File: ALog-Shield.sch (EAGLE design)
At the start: 32 parts

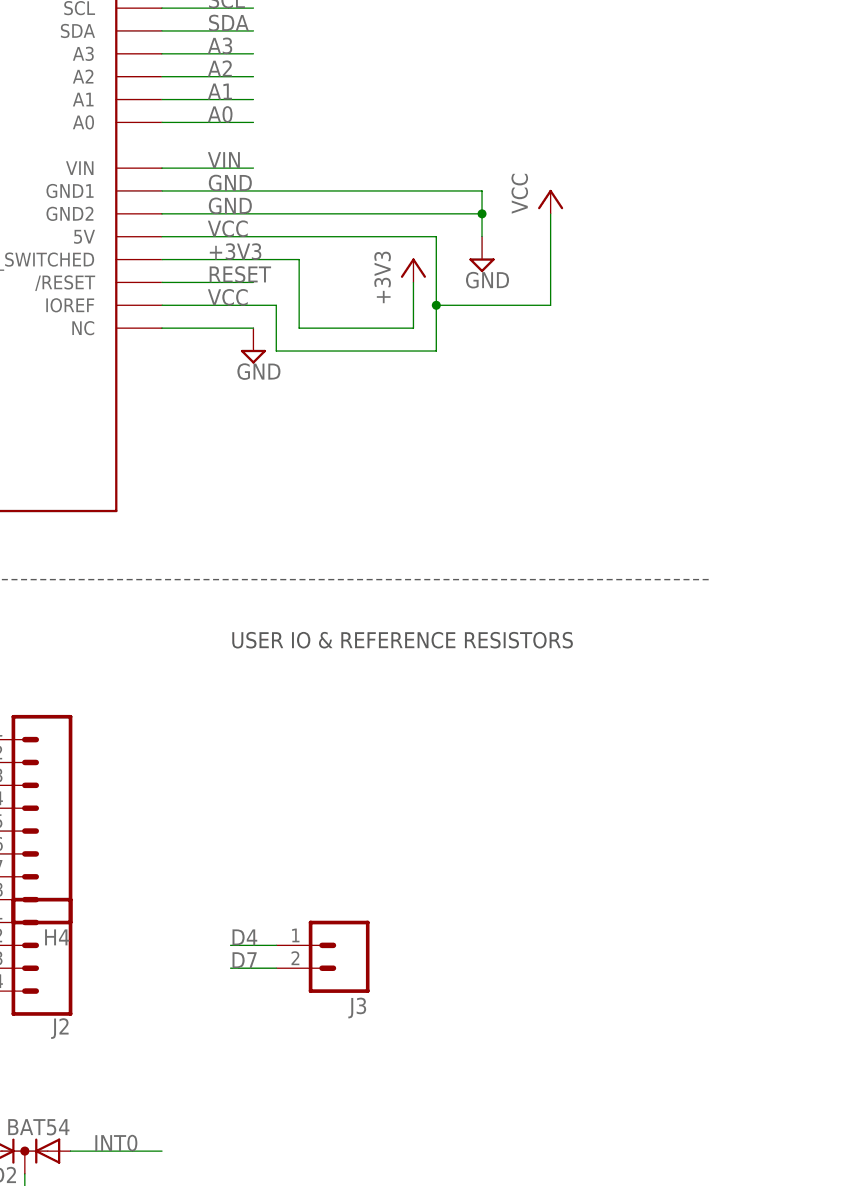
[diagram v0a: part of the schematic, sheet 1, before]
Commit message: IO Ref conversion
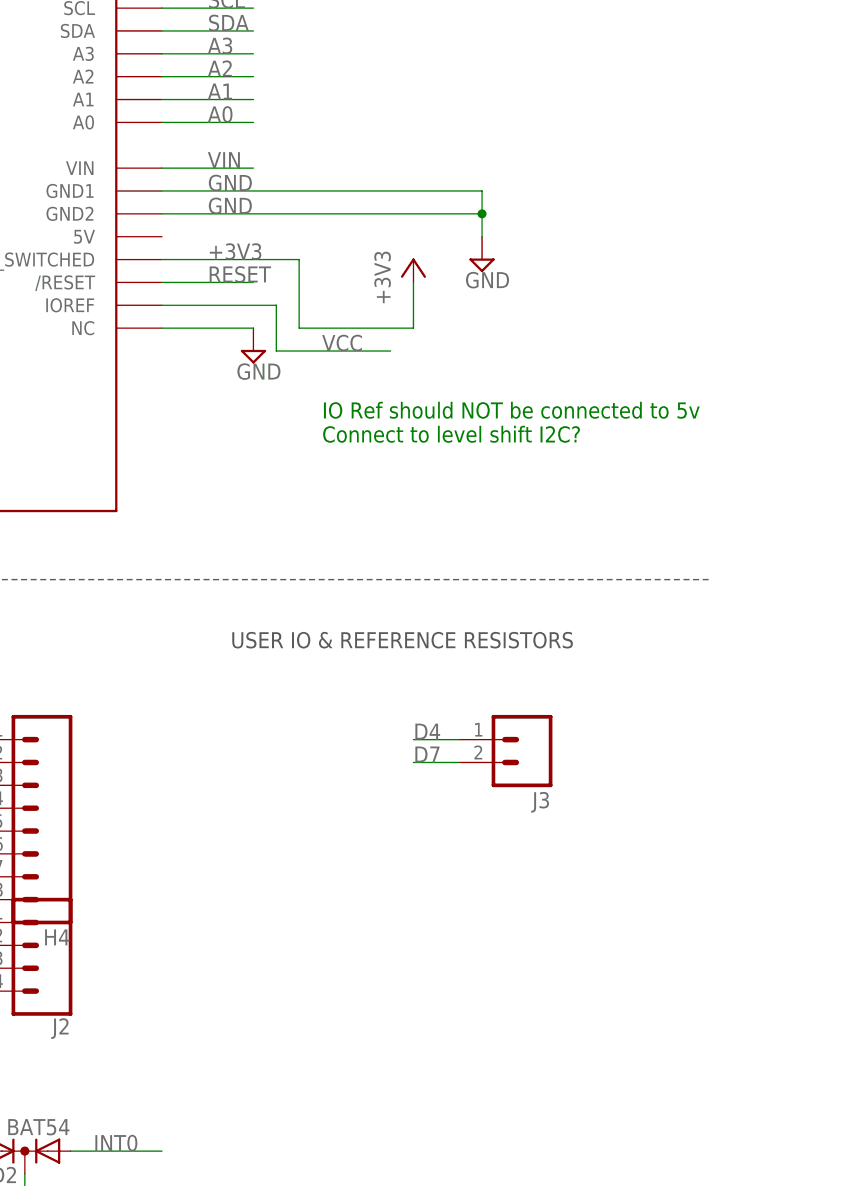
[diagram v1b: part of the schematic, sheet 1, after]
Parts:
- removed R_PU_A, R_PU_L: 10k, bschulz_passives:R-EU_10KR0603
- added R1, R2: 10k, bschulz:R-EU_R0603
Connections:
- net SCL: now also R1.1; no longer R_PU_L.2
- net SDA: now also R2.1; no longer R_PU_A.2
- net VCC: now also R1.2, R2.2; no longer R_PU_A.1, R_PU_L.1, U$9.5V
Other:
- note added: "IO Ref should NOT be connected to 5v Connect to level shift I2C?"
- note added: "If level shifters are used, these pull ups should be removed!"
- moved on the sheet: J3
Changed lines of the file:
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@@
 <?xml version="1.0" encoding="utf-8"?>
 <!DOCTYPE eagle SYSTEM "eagle.dtd">
-<eagle version="8.6.0">
+<eagle version="8.5.1">
 <drawing>
 <settings>
@@
 <part name="SUPPLY38" library="supply2" deviceset="GND" device=""/>
 <part name="SUPPLY39" library="supply2" deviceset="GND" device=""/>
-<part name="P+8" library="supply1" deviceset="VCC" device=""/>
 <part name="SUPPLY40" library="supply2" deviceset="GND" device=""/>
 <part name="+3V5" library="supply1" deviceset="+3V3" device=""/>
@@
 <part name="SUPPLY1" library="supply2" deviceset="GND" device=""/>
 <part name="P+3" library="supply1" deviceset="VCC" device=""/>
-<part name="P+5" library="supply1" deviceset="VCC" device=""/>
-<part name="P+7" library="supply1" deviceset="VCC" device=""/>
 <part name="P+9" library="supply1" deviceset="VCC" device=""/>
 <part name="H4" library="SparkFun" deviceset="M08" device="3.5MM-8"/>
@@
 <part name="JP1" library="SparkFun-Connectors" deviceset="M02" device="LOCK"/>
 <part name="+3V3" library="supply1" deviceset="+3V3" device=""/>
-<part name="R_PU_L" library="bschulz_passives" deviceset="R-EU_" device="R0603" technology="10K" value="10k"/>
-<part name="R_PU_A" library="bschulz_passives" deviceset="R-EU_" device="R0603" technology="10K" value="10k"/>
 <part name="C1" library="bschulz_passives" deviceset="C-EU" device="C0603" technology="0.1UF"/>
 <part name="C2" library="bschulz_passives" deviceset="C-EU" device="C0603" technology="0.1UF"/>
@@
 <part name="C4" library="bschulz_passives" deviceset="C-EU" device="C0603" technology="0.1UF"/>
 <part name="RTC1" library="bschulz" deviceset="DS3231M" device=""/>
+<part name="R1" library="bschulz" deviceset="R-EU_" device="R0603" value="10k"/>
+<part name="R2" library="bschulz" deviceset="R-EU_" device="R0603" value="10k"/>
+<part name="P+1" library="supply1" library_urn="urn:adsk.eagle:library:371" deviceset="VCC" device=""/>
+<part name="P+4" library="supply1" library_urn="urn:adsk.eagle:library:371" deviceset="VCC" device=""/>
 </parts>
 <sheets>
@@
 Chad Sandell</text>
 <text x="90.17" y="-222.504" size="5.08" layer="97">ALOG</text>
+<text x="142.24" y="-81.28" size="1.778" layer="91">IO Ref should NOT be connected to 5v
+Connect to level shift I2C?</text>
 </plain>
 <instances>
@@
 <instance part="SUPPLY38" gate="GND" x="35.56" y="-76.2"/>
 <instance part="SUPPLY39" gate="GND" x="160.02" y="-60.96"/>
-<instance part="P+8" gate="VCC" x="167.64" y="-53.34"/>
 <instance part="SUPPLY40" gate="GND" x="134.62" y="-71.12"/>
 <instance part="+3V5" gate="G$1" x="152.4" y="-60.96"/>
@@
 <instance part="U$3" gate="G$1" x="25.4" y="-236.22"/>
 <instance part="LOGO1" gate="G$1" x="17.78" y="-12.7"/>
-<instance part="J3" gate="G$1" x="144.78" y="-137.16" rot="R180"/>
+<instance part="J3" gate="G$1" x="165.1" y="-114.3" rot="R180"/>
 <instance part="U$1" gate="G$1" x="17.78" y="-27.94"/>
 <instance part="C1" gate="G$1" x="48.26" y="-165.1" rot="R90"/>
@@
 <net name="VCC" class="0">
 <segment>
-<wire x1="124.46" y1="-58.42" x2="154.94" y2="-58.42" width="0.1524" layer="91"/>
-<pinref part="U$9" gate="G$1" pin="5V"/>
-<label x="129.54" y="-58.42" size="1.778" layer="95"/>
-<wire x1="154.94" y1="-58.42" x2="154.94" y2="-66.04" width="0.1524" layer="91"/>
-<wire x1="154.94" y1="-66.04" x2="167.64" y2="-66.04" width="0.1524" layer="91"/>
-<wire x1="167.64" y1="-66.04" x2="167.64" y2="-55.88" width="0.1524" layer="91"/>
-<pinref part="P+8" gate="VCC" pin="VCC"/>
-<wire x1="124.46" y1="-66.04" x2="137.16" y2="-66.04" width="0.1524" layer="91"/>
-<pinref part="U$9" gate="G$1" pin="IOREF"/>
-<label x="129.54" y="-66.04" size="1.778" layer="95"/>
-<wire x1="137.16" y1="-66.04" x2="137.16" y2="-71.12" width="0.1524" layer="91"/>
-<wire x1="137.16" y1="-71.12" x2="154.94" y2="-71.12" width="0.1524" layer="91"/>
-<wire x1="154.94" y1="-71.12" x2="154.94" y2="-66.04" width="0.1524" layer="91"/>
-<junction x="154.94" y="-66.04"/>
-</segment>
-<segment>
 <label x="91.44" y="-124.46" size="1.778" layer="95"/>
 <wire x1="86.36" y1="-124.46" x2="104.14" y2="-124.46" width="0.1524" layer="91"/>
@@
 <pinref part="J1" gate="G$1" pin="1"/>
 <pinref part="P+2" gate="VCC" pin="VCC"/>
+</segment>
+<segment>
+<pinref part="U$9" gate="G$1" pin="IOREF"/>
+<wire x1="124.46" y1="-66.04" x2="137.16" y2="-66.04" width="0.1524" layer="91"/>
+<wire x1="137.16" y1="-66.04" x2="137.16" y2="-71.12" width="0.1524" layer="91"/>
+<wire x1="137.16" y1="-71.12" x2="149.86" y2="-71.12" width="0.1524" layer="91"/>
+<label x="142.24" y="-71.12" size="1.778" layer="95"/>
 </segment>
 </net>
@@
 <segment>
 <pinref part="J3" gate="G$1" pin="1"/>
-<wire x1="137.16" y1="-137.16" x2="132.08" y2="-137.16" width="0.1524" layer="91"/>
-<label x="132.08" y="-137.16" size="1.778" layer="95"/>
+<wire x1="157.48" y1="-114.3" x2="152.4" y2="-114.3" width="0.1524" layer="91"/>
+<label x="152.4" y="-114.3" size="1.778" layer="95"/>
 </segment>
 </net>
@@
 <segment>
 <pinref part="J3" gate="G$1" pin="2"/>
-<wire x1="137.16" y1="-139.7" x2="132.08" y2="-139.7" width="0.1524" layer="91"/>
-<label x="132.08" y="-139.7" size="1.778" layer="95"/>
+<wire x1="157.48" y1="-116.84" x2="152.4" y2="-116.84" width="0.1524" layer="91"/>
+<label x="152.4" y="-116.84" size="1.778" layer="95"/>
 </segment>
 </net>
@@
 <wire x1="104.14" y1="35.56" x2="104.14" y2="81.28" width="0.1524" layer="97" style="dashdot"/>
 <text x="114.3" y="76.2" size="1.778" layer="97">JUMPER: REFERENCE ANALOG TO 3V3 INSTEAD OF VCC</text>
+<text x="114.3" y="154.94" size="1.778" layer="91">If level shifters are used, these pull ups should be removed!</text>
 </plain>
 <instances>
@@
 <attribute name="DRAWING_NAME" x="101.6" y="19.05" size="2.54" layer="94"/>
 </instance>
-<instance part="P+5" gate="VCC" x="124.46" y="152.4"/>
-<instance part="P+7" gate="VCC" x="114.3" y="154.94"/>
 <instance part="P+9" gate="VCC" x="58.42" y="139.7"/>
 <instance part="CLOCK_BATT" gate="G$1" x="137.16" y="109.22" rot="R90"/>
@@
 <instance part="JP1" gate="G$1" x="129.54" y="58.42"/>
 <instance part="+3V3" gate="G$1" x="147.32" y="68.58"/>
-<instance part="R_PU_L" gate="G$1" x="114.3" y="142.24" rot="R270"/>
-<instance part="R_PU_A" gate="G$1" x="124.46" y="139.7" rot="R270"/>
 <instance part="RTC1" gate="G$1" x="78.74" y="132.08"/>
+<instance part="R1" gate="G$1" x="114.3" y="142.24" rot="R90"/>
+<instance part="R2" gate="G$1" x="124.46" y="139.7" rot="R90"/>
+<instance part="P+1" gate="VCC" x="114.3" y="152.4"/>
+<instance part="P+4" gate="VCC" x="124.46" y="149.86"/>
 </instances>
 <busses>
 </busses>
 <nets>
-<net name="VCC" class="0">
-<segment>
-<wire x1="124.46" y1="149.86" x2="124.46" y2="144.78" width="0.1524" layer="91"/>
-<pinref part="P+5" gate="VCC" pin="VCC"/>
-<pinref part="R_PU_A" gate="G$1" pin="1"/>
-</segment>
-<segment>
-<wire x1="114.3" y1="152.4" x2="114.3" y2="147.32" width="0.1524" layer="91"/>
-<pinref part="P+7" gate="VCC" pin="VCC"/>
-<pinref part="R_PU_L" gate="G$1" pin="1"/>
-</segment>
-<segment>
-<wire x1="66.04" y1="134.62" x2="58.42" y2="134.62" width="0.1524" layer="91"/>
-<wire x1="58.42" y1="134.62" x2="58.42" y2="137.16" width="0.1524" layer="91"/>
-<pinref part="P+9" gate="VCC" pin="VCC"/>
-<pinref part="RTC1" gate="G$1" pin="VCC"/>
-</segment>
-</net>
 <net name="DI" class="0">
 <segment>
@@
 </segment>
 </net>
-<net name="SCL" class="0">
-<segment>
-<wire x1="91.44" y1="137.16" x2="114.3" y2="137.16" width="0.1524" layer="91"/>
-<label x="99.06" y="137.16" size="1.778" layer="95"/>
-<pinref part="R_PU_L" gate="G$1" pin="2"/>
-<pinref part="RTC1" gate="G$1" pin="SCL"/>
-</segment>
-</net>
-<net name="SDA" class="0">
-<segment>
-<wire x1="91.44" y1="134.62" x2="124.46" y2="134.62" width="0.1524" layer="91"/>
-<label x="99.06" y="134.62" size="1.778" layer="95"/>
-<pinref part="R_PU_A" gate="G$1" pin="2"/>
-<pinref part="RTC1" gate="G$1" pin="SDA"/>
-</segment>
-</net>
 <net name="INT0" class="0">
 <segment>
@@
 </segment>
 </net>
+<net name="SCL" class="0">
+<segment>
+<wire x1="91.44" y1="137.16" x2="114.3" y2="137.16" width="0.1524" layer="91"/>
+<label x="99.06" y="137.16" size="1.778" layer="95"/>
+<pinref part="RTC1" gate="G$1" pin="SCL"/>
+<pinref part="R1" gate="G$1" pin="1"/>
+</segment>
+</net>
+<net name="SDA" class="0">
+<segment>
+<wire x1="91.44" y1="134.62" x2="124.46" y2="134.62" width="0.1524" layer="91"/>
+<label x="99.06" y="134.62" size="1.778" layer="95"/>
+<pinref part="RTC1" gate="G$1" pin="SDA"/>
+<pinref part="R2" gate="G$1" pin="1"/>
+</segment>
+</net>
+<net name="VCC" class="0">
+<segment>
+<wire x1="66.04" y1="134.62" x2="58.42" y2="134.62" width="0.1524" layer="91"/>
+<wire x1="58.42" y1="134.62" x2="58.42" y2="137.16" width="0.1524" layer="91"/>
+<pinref part="P+9" gate="VCC" pin="VCC"/>
+<pinref part="RTC1" gate="G$1" pin="VCC"/>
+</segment>
+<segment>
+<pinref part="R1" gate="G$1" pin="2"/>
+<pinref part="P+1" gate="VCC" pin="VCC"/>
+<wire x1="114.3" y1="147.32" x2="114.3" y2="149.86" width="0.1524" layer="91"/>
+</segment>
+<segment>
+<pinref part="R2" gate="G$1" pin="2"/>
+<pinref part="P+4" gate="VCC" pin="VCC"/>
+<wire x1="124.46" y1="144.78" x2="124.46" y2="147.32" width="0.1524" layer="91"/>
+</segment>
+</net>
 </nets>
 </sheet>
@@
 which will not be processed correctly with this version.
 </note>
+<note version="8.2" severity="warning">
+Since Version 8.2, EAGLE supports online libraries. The ids
+of those online libraries will not be understood (or retained)
+with this version.
+</note>
+<note version="8.3" severity="warning">
+Since Version 8.3, EAGLE supports URNs for individual library
+assets (packages, symbols, and devices). The URNs of those assets
+will not be understood (or retained) with this version.
+</note>
 </compatibility>

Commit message: PU, reroute, 5V terminal
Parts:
- removed J3: (no value), SparkFun-Connectors:M023.5MM
- added JP2: (no value), SparkFun-Connectors:M03SCREW
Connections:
- new net 5V: JP2.3, U$9.5V
- net D4: now also JP2.1; no longer J3.1
- net D7: now also JP2.2; no longer J3.2
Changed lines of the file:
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@@
 <?xml version="1.0" encoding="utf-8"?>
 <!DOCTYPE eagle SYSTEM "eagle.dtd">
-<eagle version="8.5.1">
+<eagle version="8.6.0">
 <drawing>
 <settings>
@@
 <part name="U$3" library="awickert" deviceset="ALOG_LOG" device=""/>
 <part name="LOGO1" library="SparkFun-Aesthetics" deviceset="OSHW-LOGO" device="L"/>
-<part name="J3" library="SparkFun-Connectors" deviceset="M02" device="3.5MM"/>
 <part name="+3V2" library="supply1" deviceset="+3V3" device=""/>
 <part name="+3V7" library="supply1" deviceset="+3V3" device=""/>
@@
 <part name="P+1" library="supply1" library_urn="urn:adsk.eagle:library:371" deviceset="VCC" device=""/>
 <part name="P+4" library="supply1" library_urn="urn:adsk.eagle:library:371" deviceset="VCC" device=""/>
+<part name="JP2" library="SparkFun-Connectors" deviceset="M03" device="SCREW"/>
 </parts>
 <sheets>
@@
 <instance part="U$3" gate="G$1" x="25.4" y="-236.22"/>
 <instance part="LOGO1" gate="G$1" x="17.78" y="-12.7"/>
-<instance part="J3" gate="G$1" x="165.1" y="-114.3" rot="R180"/>
 <instance part="U$1" gate="G$1" x="17.78" y="-27.94"/>
 <instance part="C1" gate="G$1" x="48.26" y="-165.1" rot="R90"/>
@@
 <instance part="C3" gate="G$1" x="48.26" y="-185.42" rot="R90"/>
 <instance part="C4" gate="G$1" x="48.26" y="-195.58" rot="R90"/>
+<instance part="JP2" gate="G$1" x="165.1" y="-116.84" rot="R180"/>
 </instances>
 <busses>
@@
 </segment>
 <segment>
-<pinref part="J3" gate="G$1" pin="1"/>
 <wire x1="157.48" y1="-114.3" x2="152.4" y2="-114.3" width="0.1524" layer="91"/>
 <label x="152.4" y="-114.3" size="1.778" layer="95"/>
+<pinref part="JP2" gate="G$1" pin="1"/>
 </segment>
 </net>
@@
 </segment>
 <segment>
-<pinref part="J3" gate="G$1" pin="2"/>
 <wire x1="157.48" y1="-116.84" x2="152.4" y2="-116.84" width="0.1524" layer="91"/>
 <label x="152.4" y="-116.84" size="1.778" layer="95"/>
+<pinref part="JP2" gate="G$1" pin="2"/>
 </segment>
 </net>
@@
 </segment>
 </net>
+<net name="5V" class="0">
+<segment>
+<pinref part="U$9" gate="G$1" pin="5V"/>
+<wire x1="124.46" y1="-58.42" x2="134.62" y2="-58.42" width="0.1524" layer="91"/>
+<label x="129.54" y="-58.42" size="1.778" layer="95"/>
+</segment>
+<segment>
+<pinref part="JP2" gate="G$1" pin="3"/>
+<wire x1="157.48" y1="-119.38" x2="152.4" y2="-119.38" width="0.1524" layer="91"/>
+<label x="152.4" y="-119.38" size="1.778" layer="95"/>
+</segment>
+</net>
